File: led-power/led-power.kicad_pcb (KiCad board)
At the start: 2 copper layers, 86.4 x 86.4 mm, 70 parts, among them J1 String1, J10 PowerInput, J2 String2, J3 String3, J4 String4, J5 String5, J6 String6, J7 String7, J8 String8, J9 PowerInput, Q1 Q_NMOS_GDS, Q2 Q_NMOS_GDS, Q3 Q_NMOS_GDS, Q4 Q_NMOS_GDS, Q5 Q_NMOS_GDS, Q6 Q_NMOS_GDS, Q7 Q_NMOS_GDS, Q8 Q_NMOS_GDS, U1 MCP6V51, U10 L78L05ACZ-AP, U11 MCP1501, U2 MCP6V51, U3 MCP6V51, U4 MCP6V51, U5 MCP6V51, U6 MCP6V51, U7 MCP6V51, U8 MCP6V51

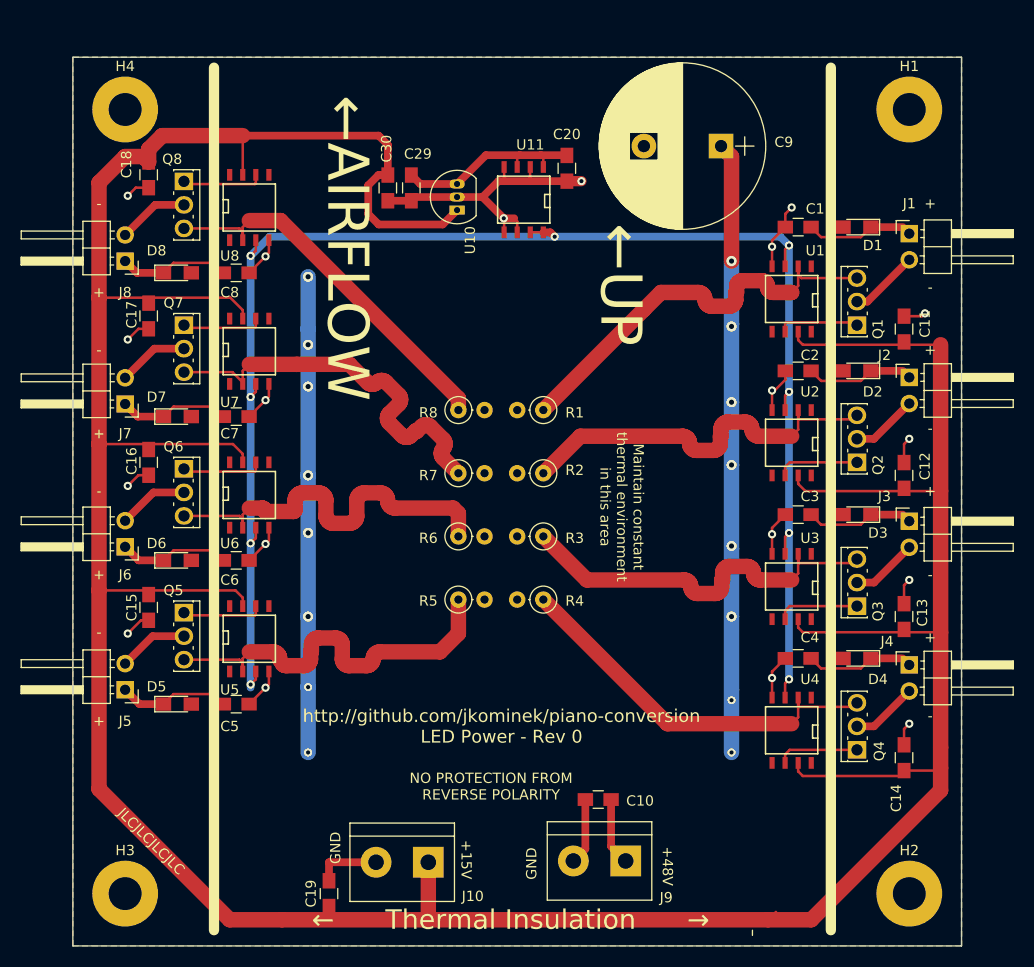
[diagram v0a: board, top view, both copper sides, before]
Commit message: Lots of LED power bring-up corrections
* MSOP-8 footprint for op amps
* TO-220 footprint for FETs
* Moved C10 away from J9
* Stopped bothering with length-adjusted traces to resistors
* Moved diodes away from LED strip terminals
* Silkscreen tweaks
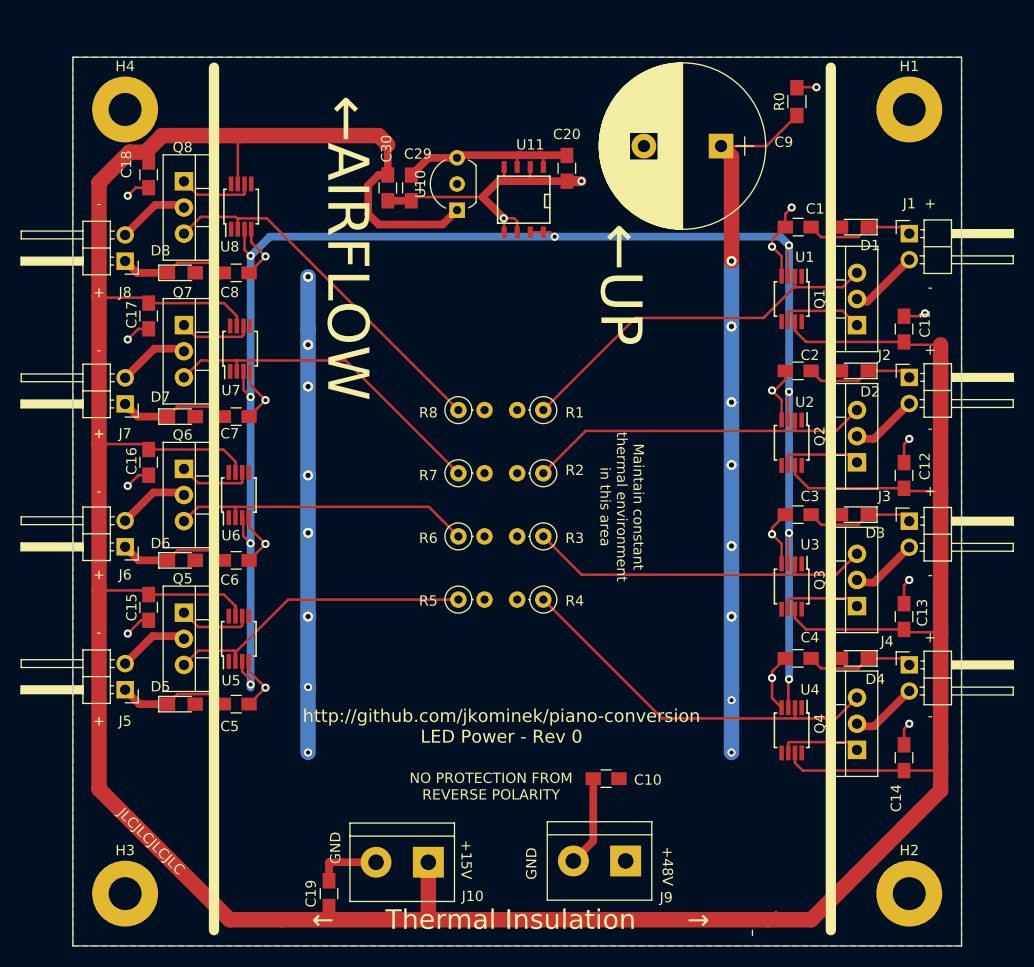
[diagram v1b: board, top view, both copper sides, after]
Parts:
- added R0: Dissipate, Resistors_SMD:R_0805_HandSoldering, F.Cu at (141.5, 75.4)
- Q1, Q2, Q3, Q4, Q5, Q6, Q7, Q8: footprint TO_SOT_Packages_THT:SIPAK_Vertical -> TO_SOT_Packages_THT:TO-220-3_Vertical
- U1, U2, U3, U4, U5, U6, U7, U8: footprint SMD_Packages:SOIC-8-N -> Housings_SSOP:MSOP-8_3x3mm_Pitch0.65mm
- U10: footprint TO_SOT_Packages_THT:TO-92_Inline_Narrow_Oval -> TO_SOT_Packages_THT:TO-92_Inline_Wide
- moved C10 2.17 mm to (122.9, 141.2)
- moved U5 1.02 mm to (87.2, 127.6), turned to 90 degrees
- moved U6 1.02 mm to (87.2, 113.7), turned to 90 degrees
- moved U7 0.92 mm to (87.4, 99.4), turned to 90 degrees
- moved U8 0.80 mm to (87.5, 85.6), turned to 90 degrees
- moved D5 0.38 mm to (81.7, 134.0)
- moved D6 0.38 mm to (81.7, 120.0)
- moved D7 0.38 mm to (81.7, 106.0)
- moved D8 0.38 mm to (81.7, 92.1)
- moved D1 0.25 mm to (147.1, 87.6)
- moved D2 0.25 mm to (147.1, 101.6)
- moved D3 0.25 mm to (147.1, 115.6)
- moved D4 0.25 mm to (147.1, 129.5)
- turned U1 to 270 degrees
- turned U2 to 270 degrees
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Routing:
- net GND: track 96.9 -> 112.6 mm, vias 19 -> 20
- net Net-(Q6-Pad3): track 38.7 -> 29.5 mm
- net Net-(Q5-Pad3): track 38.8 -> 30.6 mm
- net /VREF: track 154.8 -> 162.8 mm
- net Net-(Q7-Pad3): track 38.6 -> 32.9 mm
- net Net-(Q1-Pad3): track 42.3 -> 37.0 mm
- net Net-(Q3-Pad3): track 39.0 -> 33.9 mm
- net Net-(Q2-Pad3): track 38.9 -> 34.1 mm
- net +48V: track 112.1 -> 114.2 mm
- net Net-(Q4-Pad3): track 38.9 -> 37.4 mm
- net Net-(Q8-Pad3): track 37.4 -> 36.2 mm
- net Net-(Q7-Pad1): track 7.95 -> 7.21 mm
- net +5V: track 19.1 -> 18.4 mm
- net Net-(Q6-Pad1): track 7.95 -> 7.24 mm

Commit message: Reverse polarity diodes; Qwiic header&IO Expander
Also includes relevant connections for the IO expander to the
feedback nets, and /SHDN on the voltage reference.
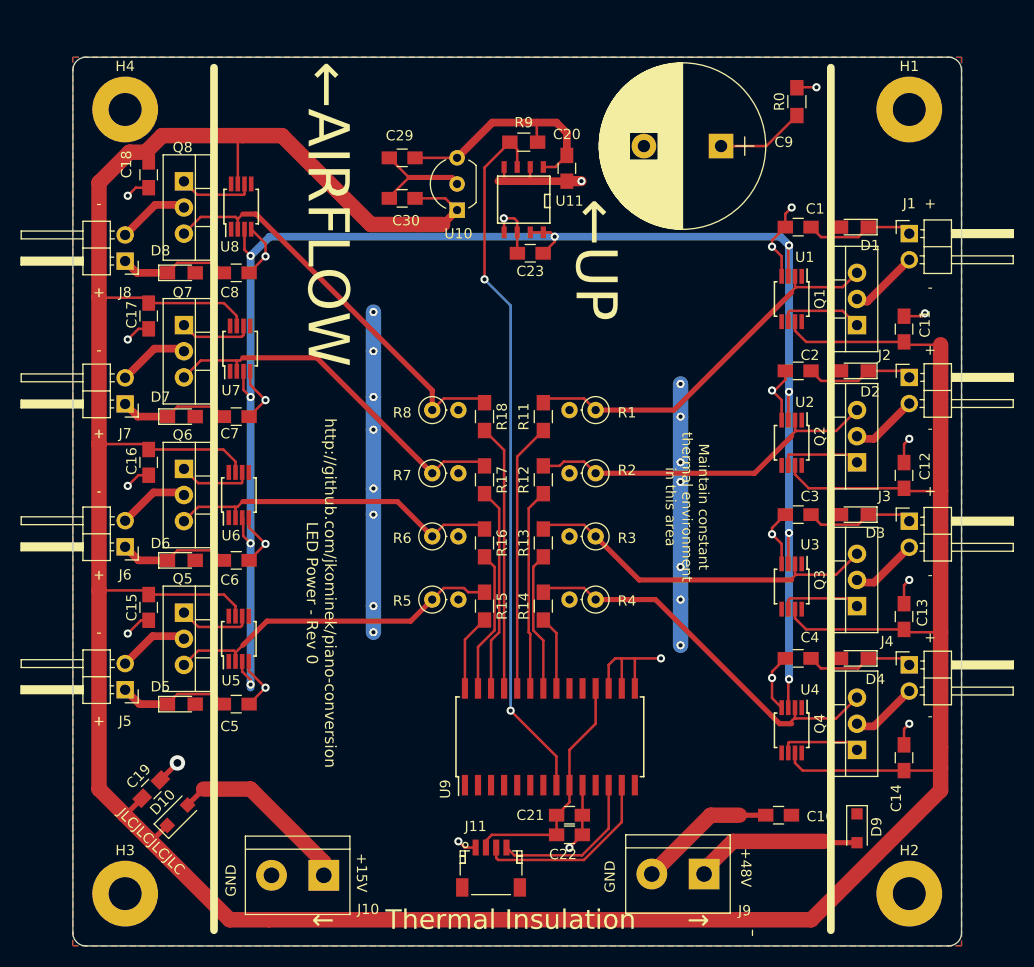
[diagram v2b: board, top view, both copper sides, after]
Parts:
- added C21: 4.7uF, Capacitors_SMD:C_0805_HandSoldering, F.Cu at (119.4, 144.8)
- added C22: 0.1uF, Capacitors_SMD:C_0805_HandSoldering, F.Cu at (119.4, 146.7)
- added C23: 300pF, Capacitors_SMD:C_0805_HandSoldering, F.Cu at (115.6, 90.2)
- added D10: D_Small_ALT, Diodes_SMD:D_SOD-123F, F.Cu at (81.3, 144.8)
- added D9: D_Small_ALT, Diodes_SMD:D_SOD-123F, F.Cu at (147.3, 146.1)
- added J11: Qwiic, Connectors_JST:JST_SH_SM04B-SRSS-TB_04x1.00mm_Angled, F.Cu at (111.8, 149.9)
- added R11: 43k, Resistors_SMD:R_0805_HandSoldering, F.Cu at (116.8, 106.0)
- added R12: 43k, Resistors_SMD:R_0805_HandSoldering, F.Cu at (116.8, 112.2)
- added R13: 43k, Resistors_SMD:R_0805_HandSoldering, F.Cu at (116.8, 118.3)
- added R14: 43k, Resistors_SMD:R_0805_HandSoldering, F.Cu at (116.8, 124.5)
- added R15: 43k, Resistors_SMD:R_0805_HandSoldering, F.Cu at (111.1, 124.5)
- added R16: 43k, Resistors_SMD:R_0805_HandSoldering, F.Cu at (111.1, 118.3)
- added R17: 43k, Resistors_SMD:R_0805_HandSoldering, F.Cu at (111.1, 112.2)
- added R18: 43k, Resistors_SMD:R_0805_HandSoldering, F.Cu at (111.1, 106.0)
- added R9: 3600, Resistors_SMD:R_0805_HandSoldering, F.Cu at (114.9, 79.4)
- added U9: MCP23017_SO, Housings_SOIC:SOIC-28W_7.5x17.9mm_Pitch1.27mm, F.Cu at (117.5, 137.2)
- moved C19 20.0 mm to (78.7, 142.2), turned to 45 degrees
- moved C10 17.1 mm to (139.7, 144.8)
- moved J10 10.2 mm to (95.5, 150.6)
- moved J9 7.73 mm to (132.5, 150.5)
- moved R1 5.08 mm to (121.9, 105.4)
- moved R2 5.08 mm to (121.9, 111.5)
- moved R3 5.08 mm to (121.9, 117.7)
- moved R4 5.08 mm to (121.9, 123.8)
- moved C29 3.05 mm to (103.1, 80.9), turned to 180 degrees
- moved R5 2.54 mm to (106.0, 123.8)
- moved R6 2.54 mm to (106.0, 117.7)
- moved R7 2.54 mm to (106.0, 111.5)
- moved R8 2.54 mm to (106.0, 105.4)
- moved C30 1.73 mm to (103.1, 84.8), turned to 180 degrees
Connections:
- net Net-(Q1-Pad3) renamed /Feedback1
- net Net-(Q2-Pad3) renamed /Feedback2
- net Net-(Q3-Pad3) renamed /Feedback3
- net Net-(Q4-Pad3) renamed /Feedback4
- net Net-(Q5-Pad3) renamed /Feedback5
- net Net-(Q6-Pad3) renamed /Feedback6
- net Net-(Q7-Pad3) renamed /Feedback7
- net Net-(Q8-Pad3) renamed /Feedback8
- J10 pad 1: +15V -> Net-(D10-Pad2)
- J9 pad 1: +48V -> Net-(D9-Pad2)
- U11 pad 3: +5V -> /~SHDN
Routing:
- net /~SHDN: track 0.00 -> 69.1 mm, vias 0 -> 2
- net +48V: track 114.2 -> 65.1 mm, vias 16 -> 15
- net Net-(R11-Pad2): track 0.00 -> 26.1 mm
- net Net-(R18-Pad2): track 0.00 -> 25.9 mm
- net +3V3: track 0.00 -> 23.6 mm
- net GND: track 112.6 -> 133.3 mm, vias 20 -> 24
- net Net-(R17-Pad2): track 0.00 -> 19.8 mm
- net Net-(R12-Pad2): track 0.00 -> 19.6 mm
- net /SDA: track 0.00 -> 18.4 mm
- net Net-(D10-Pad2): track 0.00 -> 18.1 mm
- net Net-(D9-Pad2): track 0.00 -> 16.5 mm
- net /SCL: track 0.00 -> 15.5 mm
- net Net-(R16-Pad2): track 0.00 -> 13.9 mm
- net Net-(R13-Pad2): track 0.00 -> 13.6 mm
- net Net-(R15-Pad2): track 0.00 -> 7.44 mm
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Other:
- outline, holes or cut-outs redrawn
- board text removed: "NO PROTECTION FROM REVERSE POLARITY"

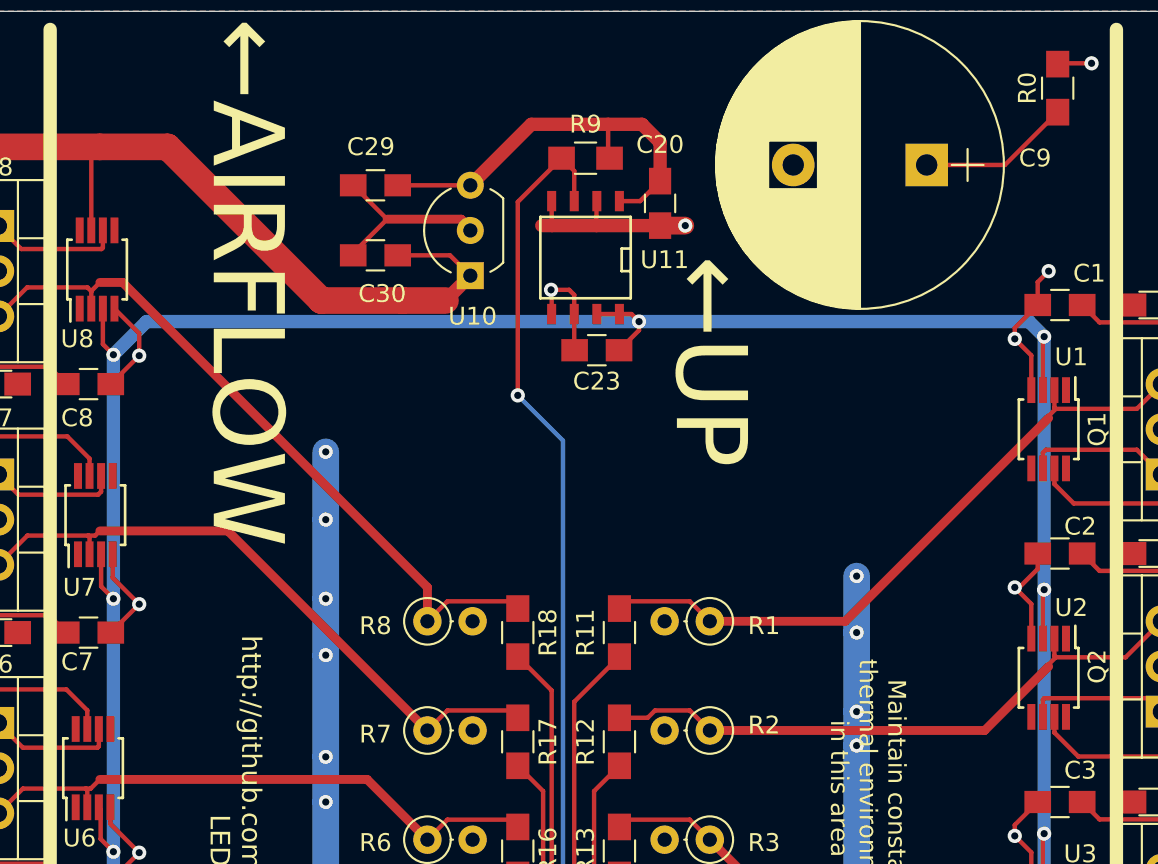
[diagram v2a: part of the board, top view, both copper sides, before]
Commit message: Correct 5V regulator orientation and give the GND pin more thermal relief.
Slightly rearranged the traces coming out of the MCP1501.
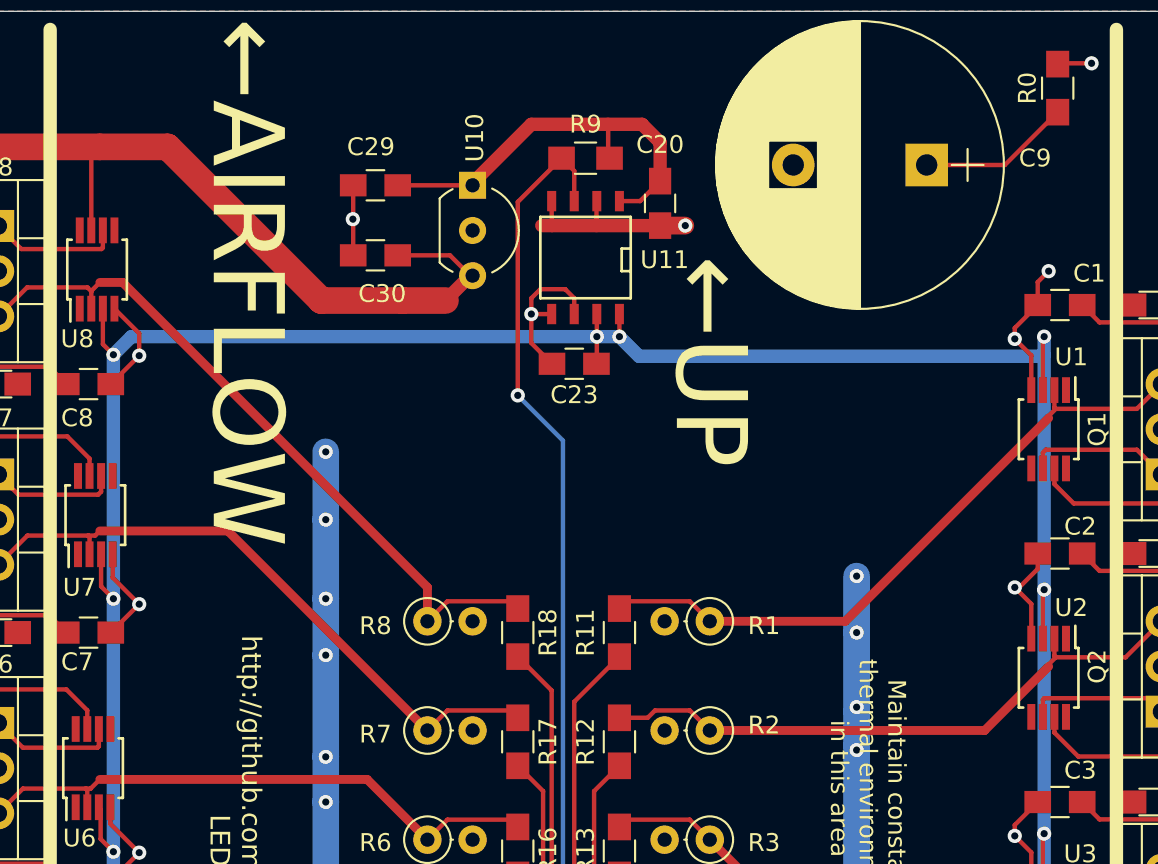
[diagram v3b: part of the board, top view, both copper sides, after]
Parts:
- moved U10 5.08 mm to (108.6, 80.9), turned to 270 degrees
- moved C23 1.48 mm to (114.3, 90.9)
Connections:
- U10 pad 1: +15V -> +5V
- U10 pad 3: +5V -> +15V
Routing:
- net GND: track 133.3 -> 130.1 mm, vias 24 -> 25
- net /VREF: track 164.9 -> 164.1 mm, vias 9 -> 10

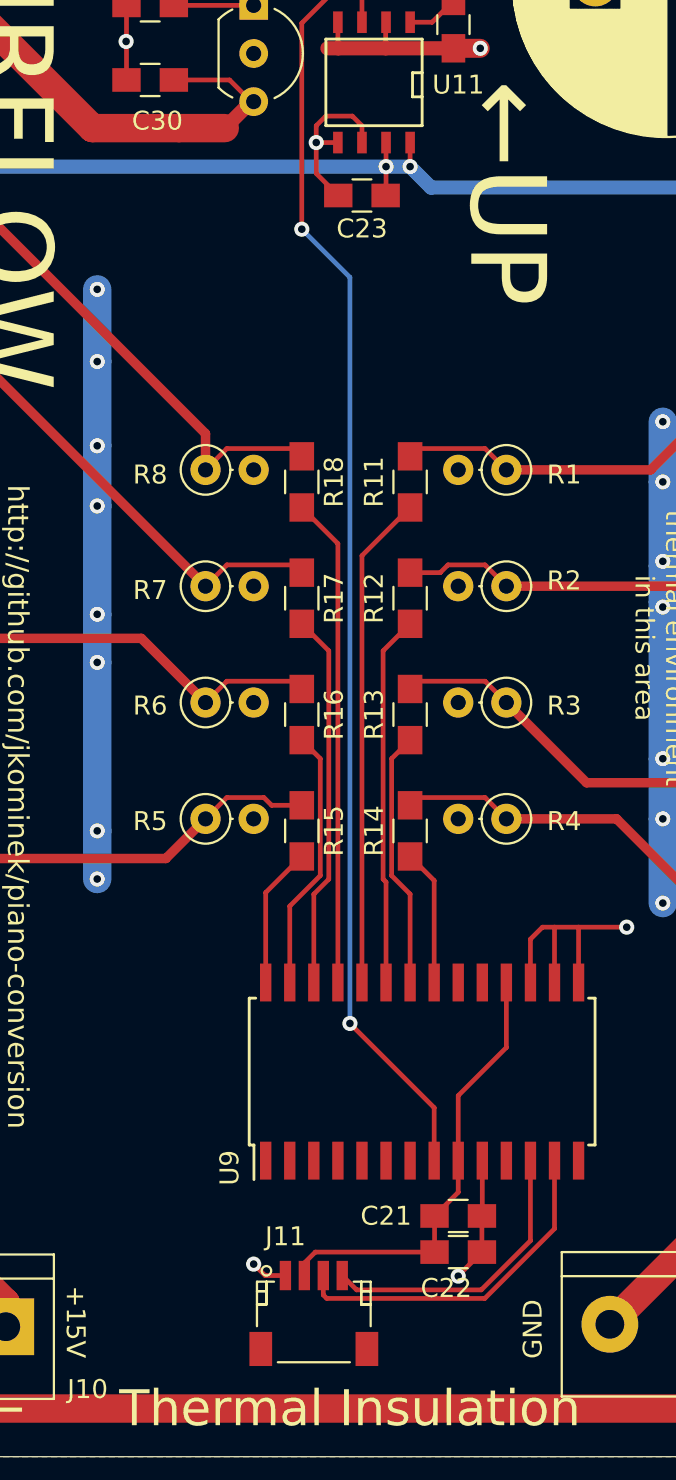
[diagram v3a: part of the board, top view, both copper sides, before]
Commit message: Add a second Qwiic header, for chaining
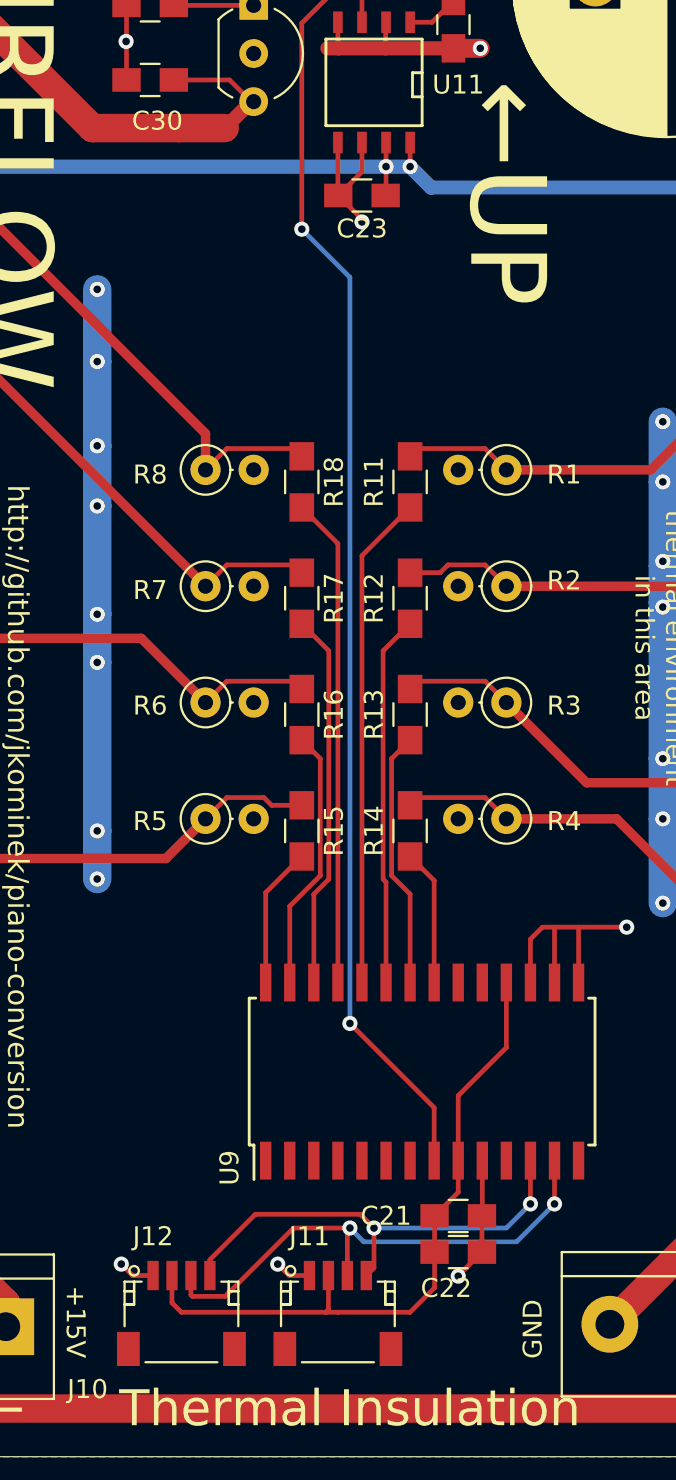
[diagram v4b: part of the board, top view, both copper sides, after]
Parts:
- added J12: Qwiic, Connectors_JST:JST_SH_SM04B-SRSS-TB_04x1.00mm_Angled, F.Cu at (104.8, 149.9)
- moved J11 1.27 mm to (113.0, 149.9)
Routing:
- net +3V3: track 23.6 -> 36.4 mm
- net /SDA: track 18.4 -> 27.7 mm, vias 0 -> 2
- net /SCL: track 15.5 -> 24.5 mm, vias 0 -> 2
- net GND: track 130.1 -> 131.0 mm, vias 25 -> 26
